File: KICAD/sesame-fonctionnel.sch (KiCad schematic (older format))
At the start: 2 parts, among them J1 Screw_Terminal_01x04, J2 Screw_Terminal_01x04

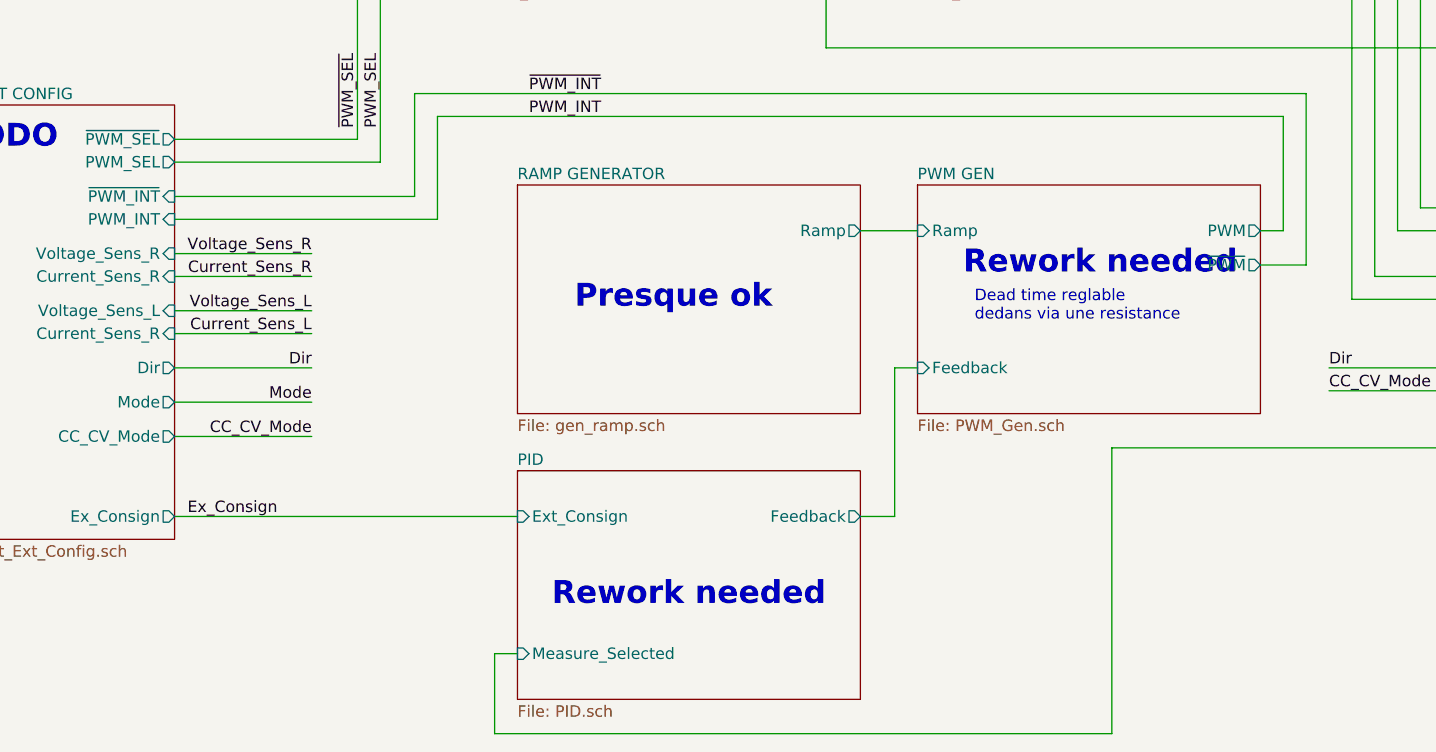
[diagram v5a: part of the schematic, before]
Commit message: PID + PWM + RAMP finished
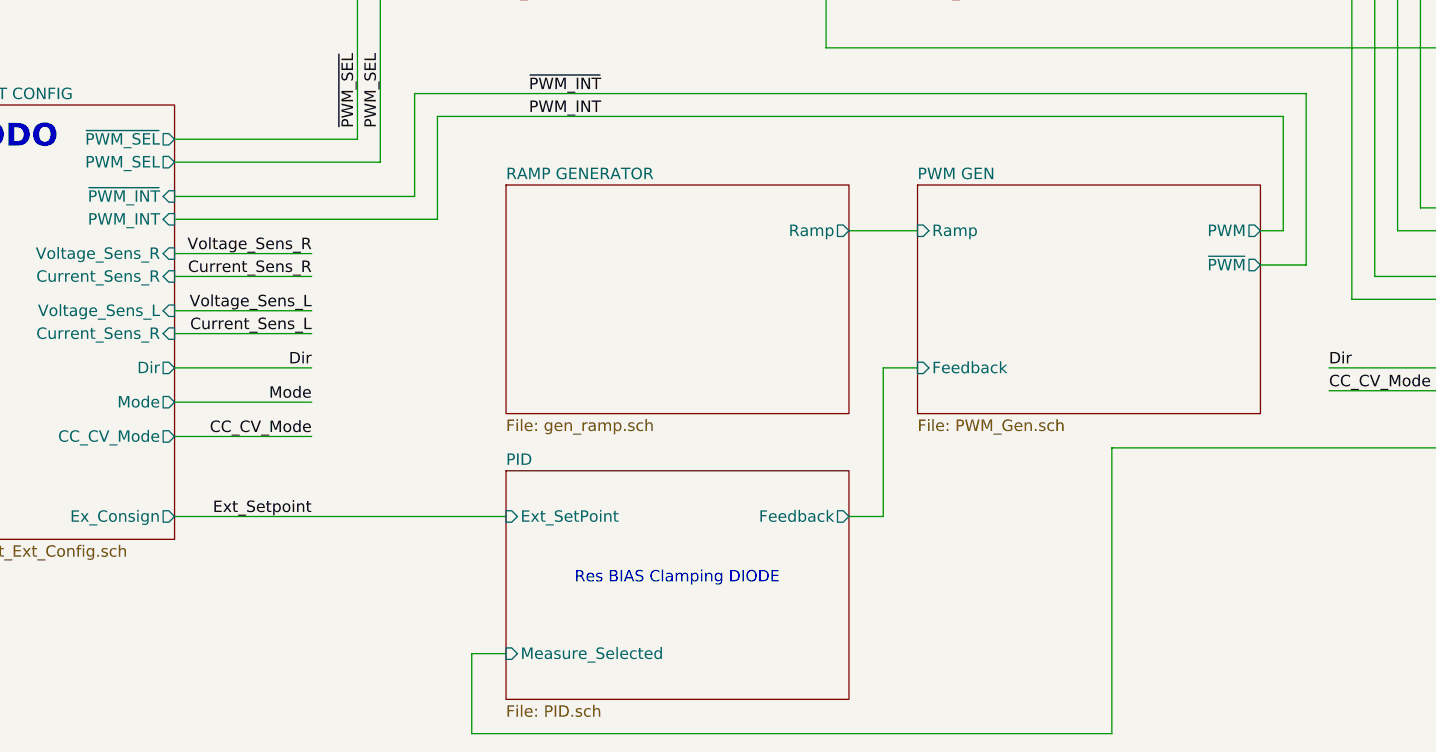
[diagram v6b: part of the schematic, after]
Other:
- note added: "Res BIAS Clamping DIODE"
- note removed: "Dead time reglable\ndedans via une resistance"
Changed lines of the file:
@@
 $EndDescr
-$Sheet
-S 3350 5350 1500 1000
-U 60F16FAE
-F0 "RAMP GENERATOR" 50
-F1 "gen_ramp.sch" 50
-F2 "Ramp" O R 4850 5550 50
-$EndSheet
 $Sheet
 S 7400 1950 1300 1000
@@
 	6600 5700 6800 5700
 Wire Wire Line
-	4850 5550 5100 5550
-Wire Wire Line
-	5100 6150 5000 6150
-Wire Wire Line
-	5000 6150 5000 6800
-Wire Wire Line
-	5000 6800 4850 6800
-Wire Wire Line
-	3350 7400 3250 7400
-Wire Wire Line
-	3250 7400 3250 7750
+	4800 5550 5100 5550
+Wire Wire Line
+	5100 6150 4950 6150
+Wire Wire Line
+	4950 6150 4950 6800
+Wire Wire Line
+	4950 6800 4800 6800
+Wire Wire Line
+	3300 7400 3150 7400
+Wire Wire Line
+	3150 7400 3150 7750
 Wire Wire Line
 	7400 5550 7200 5550
@@
 	5950 6500 5950 7750
 Wire Wire Line
-	3250 7750 5950 7750
+	3150 7750 5950 7750
 $Sheet
 S 9000 1950 1650 500
@@
 F3 "VProt" B L 9000 2200 100
 $EndSheet
-Text Notes 5350 5950 0    50   ~ 0
-Dead time reglable\ndedans via une resistance
 Wire Wire Line
 	4450 1750 4450 2400
@@
 Over_UI_Protection
 $Sheet
-S 3350 6600 1500 1000
+S 3300 6600 1500 1000
 U 60F1B237
 F0 "PID" 50
 F1 "PID.sch" 50
-F2 "Feedback" O R 4850 6800 50
-F3 "Measure_Selected" I L 3350 7400 50
-F4 "Ext_Consign" I L 3350 6800 50
+F2 "Feedback" O R 4800 6800 50
+F3 "Measure_Selected" I L 3300 7400 50
+F4 "Ext_SetPoint" I L 3300 6800 50
 $EndSheet
 $Sheet
@@
 	6600 2200 7400 2200
 Wire Wire Line
-	1850 6800 3350 6800
-Text Label 2300 6800 2    50   ~ 0
-Ex_Consign
+	1850 6800 3300 6800
+Text Label 2450 6800 2    50   ~ 0
+Ext_Setpoint
 $Sheet
 S 3050 1950 1300 1000
@@
 Text Notes 3250 3650 0    100  ~ 20
 Rework needed
-Text Notes 3600 5900 0    100  ~ 20
-Presque ok
 Text Notes 9950 5550 0    100  ~ 20
 Presque ok
@@
 Wire Wire Line
 	6700 3650 6700 2700
-Text Notes 5300 5750 0    100  ~ 20
-Rework needed
-Text Notes 3500 7200 0    100  ~ 20
-Rework needed
 Text Notes 5250 4400 0    100  ~ 20
 Trouver Driver
@@
 F1 "infos.sch" 100
 $EndSheet
+$Sheet
+S 3300 5350 1500 1000
+U 60F16FAE
+F0 "RAMP GENERATOR" 50
+F1 "gen_ramp.sch" 50
+F2 "Ramp" O R 4800 5550 50
+$EndSheet
+Text Notes 3600 7100 0    50   ~ 0
+Res BIAS Clamping DIODE
 $EndSCHEMATC

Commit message: worked on power supply + connectors
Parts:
- removed J1: Screw_Terminal_01x04, symbol Connector:Screw_Terminal_01x04
- added H? (x2): MountingHole_Pad, symbol Mechanical:MountingHole_Pad
- added J? (x2): Screw_Terminal_01x01, symbol Connector:Screw_Terminal_01x01
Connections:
- net GND: now also H?.1, J?.1 (Pin_1)
- net LEFT PROTECTION/IN_OUT_PWR: now also H?.1, J?.1 (Pin_1)
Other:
- note added: "Calculs SEPIC"
- note added: "Johnson / Cinch Connectivity Solutions 108-0740-102\nor Keystone 6095\n+ CXS70-14-C"
- note removed: "A finir choix aop"
- note removed: "Ok"
- note removed: "Presque ok"
- note removed: "Rails d’alim 7V"
- note removed: "Rework needed"
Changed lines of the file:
@@
 F4 "Current_Sens" O L 7400 2400 50
 F5 "Voltage_Sens" O L 7400 2500 50
-F6 "Dir" I R 8700 2800 50
 $EndSheet
 $Sheet
@@
 Wire Wire Line
 	4550 1850 4550 2500
-Connection ~ 900  2500
-Wire Wire Line
-	900  2400 900  2500
-Wire Wire Line
-	800  2400 900  2400
-Wire Wire Line
-	900  2500 800  2500
-Wire Wire Line
-	900  2550 900  2500
 $Comp
 L power:GND #PWR0104
 U 1 1 60FAC5D8
-P 900 2550
-F 0 "#PWR0104" H 900 2300 50  0001 C CNN
-F 1 "GND" H 905 2377 50  0000 C CNN
-F 2 "" H 900 2550 50  0001 C CNN
-F 3 "" H 900 2550 50  0001 C CNN
-	1    900  2550
+P 1150 2950
+F 0 "#PWR0104" H 1150 2700 50  0001 C CNN
+F 1 "GND" H 1150 2800 50  0000 C CNN
+F 2 "" H 1150 2950 50  0001 C CNN
+F 3 "" H 1150 2950 50  0001 C CNN
+	1    1150 2950
 	-1   0    0    -1
 $EndComp
-Connection ~ 900  2200
-Wire Wire Line
-	900  2300 900  2200
-Wire Wire Line
-	800  2300 900  2300
-Wire Wire Line
-	800  2200 900  2200
-$Comp
-L Connector:Screw_Terminal_01x04 J1
-U 1 1 60FAC5CD
-P 600 2300
-F 0 "J1" H 550 1950 50  0000 L CNN
-F 1 "Screw_Terminal_01x04" V 600 2550 50  0000 L CNN
-F 2 "" H 600 2300 50  0001 C CNN
-F 3 "~" H 600 2300 50  0001 C CNN
-	1    600  2300
-	-1   0    0    -1
-$EndComp
 Wire Wire Line
 	2900 4950 6800 4950
@@
 Wire Wire Line
 	10650 2200 10800 2200
-Wire Wire Line
-	900  2200 1050 2200
 Text Label 3350 1550 0    50   ~ 0
 VProt_Left
@@
 F4 "Current_Sens" O R 4350 2400 50
 F5 "Voltage_Sens" O R 4350 2500 50
-F6 "Dir" I L 3050 2800 50
 $EndSheet
 Wire Wire Line
@@
 	2900 1550 4950 1550
 Connection ~ 2900 2200
-Text Label 2700 2800 0    50   ~ 0
-Dir
-Wire Wire Line
-	2700 2800 3050 2800
 Wire Wire Line
 	9000 2200 8850 2200
@@
 	8850 2200 8700 2200
 Connection ~ 8850 2200
-Text Label 9050 2800 2    50   ~ 0
-Dir
-Wire Wire Line
-	9050 2800 8700 2800
-Text Notes 5450 900  0    100  ~ 20
-TODO
-Text Notes 3250 3650 0    100  ~ 20
-Rework needed
-Text Notes 9950 5550 0    100  ~ 20
-Presque ok
-Text Notes 8500 5550 0    100  ~ 20
-Ok
-Text Notes 5550 2150 0    100  ~ 20
-Ok
-Text Notes 3050 2100 0    100  ~ 20
-A finir choix aop
+Text Notes 5150 900  0    100  ~ 20
+Calculs SEPIC
 Text Notes 900  5200 0    100  ~ 20
 TODO
-Text Notes 5400 1000 0    50   ~ 10
-Rails d’alim 7V
 Wire Wire Line
 	4950 3550 4750 3550
@@
 Text Notes 5250 4400 0    100  ~ 20
 Trouver Driver
-Text Notes 7400 2100 0    100  ~ 20
-A finir choix aop
 $Sheet
 S 650  700  500  150
@@
 Text Notes 3600 7100 0    50   ~ 0
 Res BIAS Clamping DIODE
+Text Notes 550  3550 0    50   ~ 0
+Johnson / Cinch Connectivity Solutions 108-0740-102\nor Keystone 6095\n+ CXS70-14-C
+Wire Wire Line
+	800  2200 850  2200
+Wire Wire Line
+	750  2350 850  2350
+Wire Wire Line
+	850  2350 850  2200
+Connection ~ 850  2200
+Wire Wire Line
+	850  2200 1050 2200
+$Comp
+L power:GNDPWR #PWR?
+U 1 1 6140956C
+P 850 2950
+F 0 "#PWR?" H 850 2750 50  0001 C CNN
+F 1 "GNDPWR" H 850 2800 50  0000 C CNN
+F 2 "" H 850 2900 50  0001 C CNN
+F 3 "" H 850 2900 50  0001 C CNN
+	1    850  2950
+	1    0    0    -1
+$EndComp
+$Comp
+L Connector:Screw_Terminal_01x01 J?
+U 1 1 61427119
+P 600 2200
+F 0 "J?" H 1300 2100 50  0000 C CNN
+F 1 "Screw_Terminal_01x01" H 1250 2200 50  0000 C CNN
+F 2 "" H 600 2200 50  0001 C CNN
+F 3 "~" H 600 2200 50  0001 C CNN
+	1    600  2200
+	-1   0    0    1
+$EndComp
+$Comp
+L Mechanical:MountingHole_Pad H?
+U 1 1 6142711F
+P 650 2350
+F 0 "H?" V 700 3100 50  0000 C CNN
+F 1 "MountingHole_Pad" V 600 3050 50  0000 C CNN
+F 2 "" H 650 2350 50  0001 C CNN
+F 3 "~" H 650 2350 50  0001 C CNN
+	1    650  2350
+	0    -1   -1   0
+$EndComp
+$Comp
+L Connector:Screw_Terminal_01x01 J?
+U 1 1 6142C002
+P 600 2800
+F 0 "J?" H 1300 2800 50  0000 C CNN
+F 1 "Screw_Terminal_01x01" H 1250 2850 50  0000 C CNN
+F 2 "" H 600 2800 50  0001 C CNN
+F 3 "~" H 600 2800 50  0001 C CNN
+	1    600  2800
+	-1   0    0    1
+$EndComp
+$Comp
+L Mechanical:MountingHole_Pad H?
+U 1 1 6142C008
+P 650 2650
+F 0 "H?" V 700 3400 50  0000 C CNN
+F 1 "MountingHole_Pad" V 600 3350 50  0000 C CNN
+F 2 "" H 650 2650 50  0001 C CNN
+F 3 "~" H 650 2650 50  0001 C CNN
+	1    650  2650
+	0    -1   -1   0
+$EndComp
+Wire Wire Line
+	750  2650 850  2650
+Wire Wire Line
+	850  2650 850  2800
+Wire Wire Line
+	850  2800 800  2800
+Wire Wire Line
+	850  2800 850  2900
+Connection ~ 850  2800
+Wire Wire Line
+	1150 2950 1150 2900
+Wire Wire Line
+	1150 2900 850  2900
+Connection ~ 850  2900
+Wire Wire Line
+	850  2900 850  2950
 $EndSCHEMATC

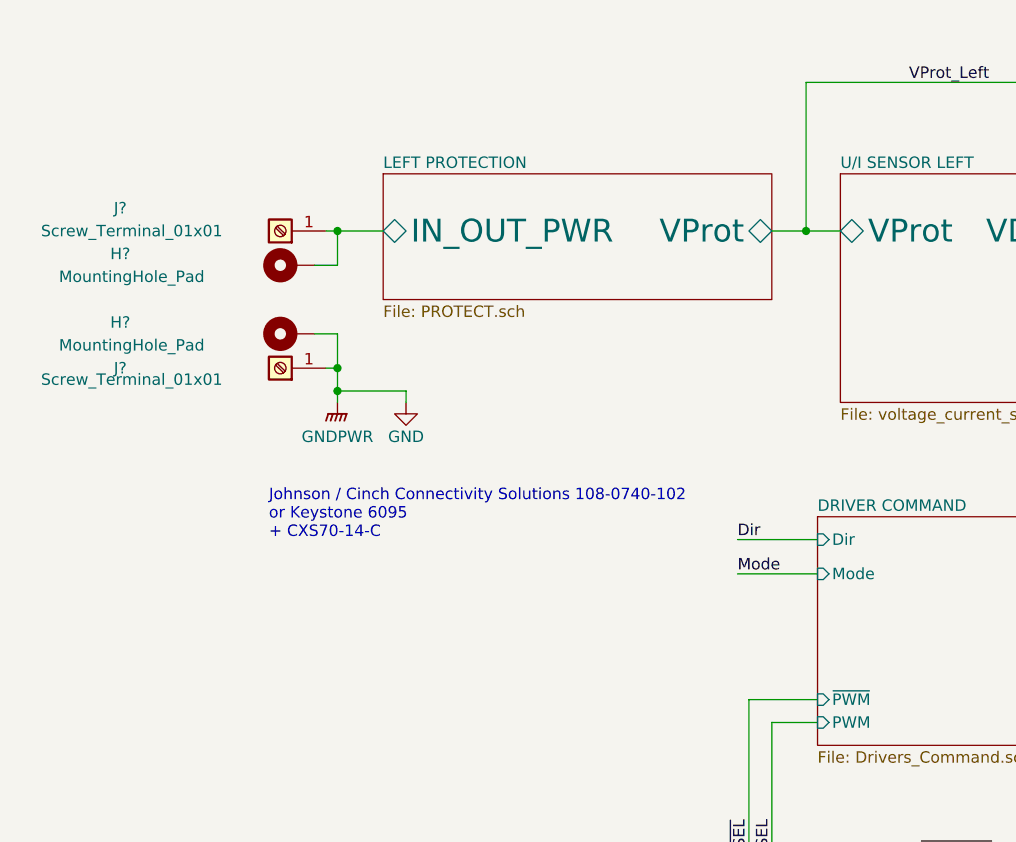
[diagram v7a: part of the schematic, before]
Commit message: added footprint lib + steps for connectors
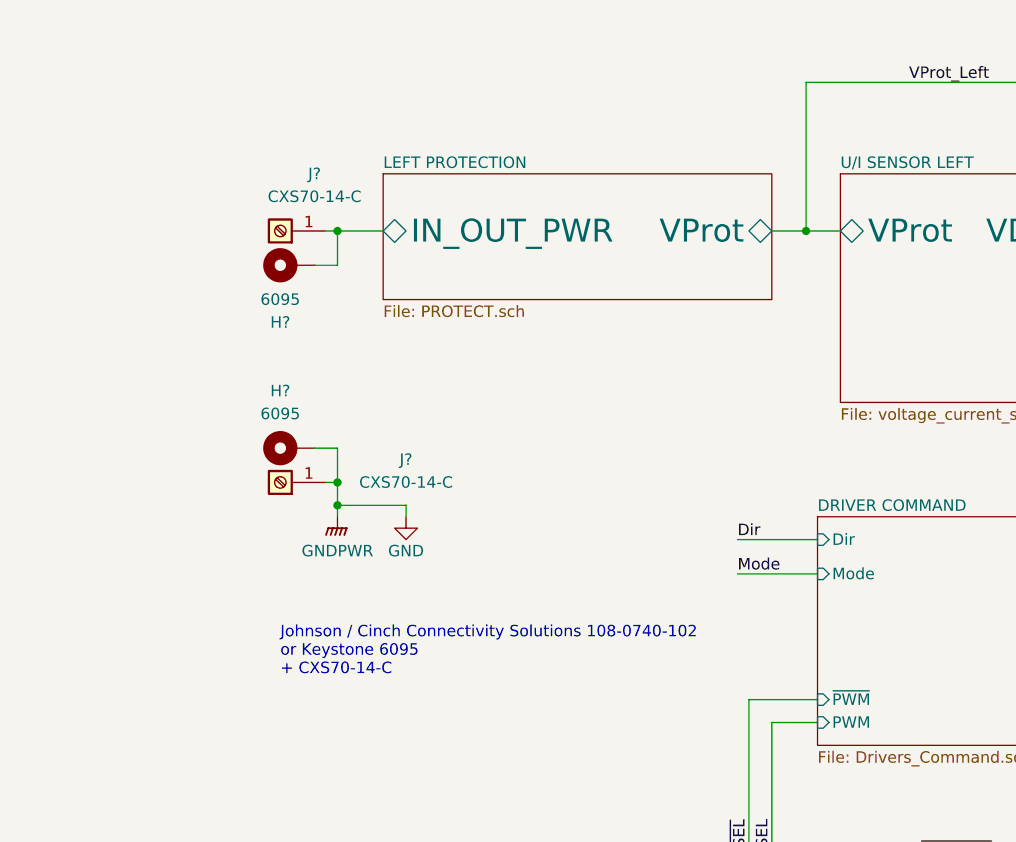
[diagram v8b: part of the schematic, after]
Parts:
- H? (x2): value MountingHole_Pad -> 6095
- J?: value Screw_Terminal_01x01 -> CXS70-14-C; footprint (none) -> Sesame_footprint:CXS70-14-C
- J?: value Screw_Terminal_01x01 -> CXS70-14-C
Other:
- moved on the sheet: H?, J?
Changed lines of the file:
@@
 L power:GND #PWR0104
 U 1 1 60FAC5D8
-P 1150 2950
-F 0 "#PWR0104" H 1150 2700 50  0001 C CNN
-F 1 "GND" H 1150 2800 50  0000 C CNN
-F 2 "" H 1150 2950 50  0001 C CNN
-F 3 "" H 1150 2950 50  0001 C CNN
-	1    1150 2950
+P 1150 3450
+F 0 "#PWR0104" H 1150 3200 50  0001 C CNN
+F 1 "GND" H 1150 3300 50  0000 C CNN
+F 2 "" H 1150 3450 50  0001 C CNN
+F 3 "" H 1150 3450 50  0001 C CNN
+	1    1150 3450
 	-1   0    0    -1
 $EndComp
@@
 Text Notes 3600 7100 0    50   ~ 0
 Res BIAS Clamping DIODE
-Text Notes 550  3550 0    50   ~ 0
+Text Notes 600  4150 0    50   ~ 0
 Johnson / Cinch Connectivity Solutions 108-0740-102\nor Keystone 6095\n+ CXS70-14-C
 Wire Wire Line
@@
 L power:GNDPWR #PWR?
 U 1 1 6140956C
-P 850 2950
-F 0 "#PWR?" H 850 2750 50  0001 C CNN
-F 1 "GNDPWR" H 850 2800 50  0000 C CNN
-F 2 "" H 850 2900 50  0001 C CNN
-F 3 "" H 850 2900 50  0001 C CNN
-	1    850  2950
+P 850 3450
+F 0 "#PWR?" H 850 3250 50  0001 C CNN
+F 1 "GNDPWR" H 850 3300 50  0000 C CNN
+F 2 "" H 850 3400 50  0001 C CNN
+F 3 "" H 850 3400 50  0001 C CNN
+	1    850  3450
 	1    0    0    -1
 $EndComp
@@
 U 1 1 61427119
 P 600 2200
-F 0 "J?" H 1300 2100 50  0000 C CNN
-F 1 "Screw_Terminal_01x01" H 1250 2200 50  0000 C CNN
-F 2 "" H 600 2200 50  0001 C CNN
+F 0 "J?" H 450 1950 50  0000 C CNN
+F 1 "CXS70-14-C" H 450 2050 50  0000 C CNN
+F 2 "Sesame_footprint:CXS70-14-C" H 600 2200 50  0001 C CNN
 F 3 "~" H 600 2200 50  0001 C CNN
 	1    600  2200
@@
 U 1 1 6142711F
 P 650 2350
-F 0 "H?" V 700 3100 50  0000 C CNN
-F 1 "MountingHole_Pad" V 600 3050 50  0000 C CNN
+F 0 "H?" V 400 2400 50  0000 C CNN
+F 1 "6095" V 500 2400 50  0000 C CNN
 F 2 "" H 650 2350 50  0001 C CNN
 F 3 "~" H 650 2350 50  0001 C CNN
@@
 L Connector:Screw_Terminal_01x01 J?
 U 1 1 6142C002
-P 600 2800
-F 0 "J?" H 1300 2800 50  0000 C CNN
-F 1 "Screw_Terminal_01x01" H 1250 2850 50  0000 C CNN
-F 2 "" H 600 2800 50  0001 C CNN
-F 3 "~" H 600 2800 50  0001 C CNN
-	1    600  2800
+P 600 3300
+F 0 "J?" H 50  3200 50  0000 C CNN
+F 1 "CXS70-14-C" H 50  3300 50  0000 C CNN
+F 2 "" H 600 3300 50  0001 C CNN
+F 3 "~" H 600 3300 50  0001 C CNN
+	1    600  3300
 	-1   0    0    1
 $EndComp
@@
 L Mechanical:MountingHole_Pad H?
 U 1 1 6142C008
-P 650 2650
-F 0 "H?" V 700 3400 50  0000 C CNN
-F 1 "MountingHole_Pad" V 600 3350 50  0000 C CNN
-F 2 "" H 650 2650 50  0001 C CNN
-F 3 "~" H 650 2650 50  0001 C CNN
-	1    650  2650
+P 650 3150
+F 0 "H?" V 900 3200 50  0000 C CNN
+F 1 "6095" V 800 3200 50  0000 C CNN
+F 2 "" H 650 3150 50  0001 C CNN
+F 3 "~" H 650 3150 50  0001 C CNN
+	1    650  3150
 	0    -1   -1   0
 $EndComp
 Wire Wire Line
-	750  2650 850  2650
-Wire Wire Line
-	850  2650 850  2800
-Wire Wire Line
-	850  2800 800  2800
-Wire Wire Line
-	850  2800 850  2900
-Connection ~ 850  2800
-Wire Wire Line
-	1150 2950 1150 2900
-Wire Wire Line
-	1150 2900 850  2900
-Connection ~ 850  2900
-Wire Wire Line
-	850  2900 850  2950
+	750  3150 850  3150
+Wire Wire Line
+	850  3150 850  3300
+Wire Wire Line
+	850  3300 800  3300
+Wire Wire Line
+	850  3300 850  3400
+Connection ~ 850  3300
+Wire Wire Line
+	1150 3450 1150 3400
+Wire Wire Line
+	1150 3400 850  3400
+Connection ~ 850  3400
+Wire Wire Line
+	850  3400 850  3450
 $EndSCHEMATC
